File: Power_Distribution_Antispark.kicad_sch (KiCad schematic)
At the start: 155 parts, among them J1 5V Output 2, J10 +48V Battery Conn, J2 Adjustable Output, J3 Motor Conn, J4 12V Output 2, J5 Conn_01x14_Socket, J6 STM_Adj_En, J7 12V Output 1, J8 5V Output 1, J9 STM Conn, Q10 GSF3400, Q11 GSF3400, Q4 BUK9M42-60EX, Q6 GSF3400, Q7 G20P06K, Q8 BUK9M42-60EX, Q9 G20P06K, U1 MCP1792x-5002xDB, U10 INA181A3IDBVR, U11 INA181A3IDBVR, U12 INA181A3IDBVR, U13 INA181A3IDBVR, U15 SN74AHC1G02, U2 TPP60308-ES1R-S, U3 TPP60308-ES1R-S, U4 TPP60308-ES1R-S, U6 TLV74033PDBVR, U7 MCP6L01Rx-xOT, U8 INA181A3IDBVR, U9 INA181A3IDBVR

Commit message: schematic for review
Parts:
- removed F6: Fuse, symbol Device:Fuse
- added F5: 0679L9150-05, CustomFootprintLibrary:FUSC6125X279N-0679L9150-05, symbol CustomLibrary:0679L9150-05
- L1: value 8.2uH -> 6.8uH
- L2: value 8.2uH -> 15uH; footprint (none) -> CustomFootprintLibrary:IND_AMRM00101040_PUL-AMRM00101040150MA1
- L4: value 8.2uH -> 18uH
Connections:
- net +48V: now also F5.1
- net at D15.2 (A): now also F5.2
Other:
- note added: "I_ripplecurrent = 0.3*I_outmax = 0.3*3.5 = 1.05 13.7uH -> 15uH"
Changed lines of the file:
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@@
 		)
 	)
+	(text "I_ripplecurrent = 0.3*I_outmax = 0.3*3.5 = 1.05\n13.7uH -> 15uH"
+		(exclude_from_sim no)
+		(at 189.992 132.588 0)
+		(effects
+			(font
+				(size 1.27 1.27)
+			)
+		)
+	)
 	(text "Vout=0.8*(1+R1/R2)"
 		(exclude_from_sim no)
@@
 	(wire
 		(pts
-			(xy 39.37 43.18) (xy 45.72 43.18)
+			(xy 31.75 43.18) (xy 38.1 43.18)
 		)
 		(stroke
@@
 			)
 		)
-		(property "Value" "8.2uH"
+		(property "Value" "18uH"
 			(at 179.07 285.75 90)
 			(effects
@@
 			)
 		)
-		(property "Datasheet" "~"
+		(property "Datasheet" "https://www.digikey.ca/en/products/detail/vishay-dale/IFDC5050HZER180M/22475119"
 			(at 179.07 288.29 0)
 			(effects
@@
 			)
 		)
-		(property "Description" "Inductor, small symbol"
+		(property "Description" "FIXED IND 18UH 6.6A 39 MOHM SMD"
 			(at 179.07 288.29 0)
 			(effects
@@
 	(symbol
 		(lib_id "power:+48V")
-		(at 39.37 43.18 0)
+		(at 31.75 43.18 0)
 		(unit 1)
 		(exclude_from_sim no)
@@
 		(fields_autoplaced yes)
 		(property "Reference" "#PWR077"
-			(at 39.37 46.99 0)
+			(at 31.75 46.99 0)
 			(effects
 				(font
@@
 		)
 		(property "Value" "+48V"
-			(at 39.37 38.1 0)
+			(at 31.75 38.1 0)
 			(effects
 				(font
@@
 		)
 		(property "Footprint" ""
-			(at 39.37 43.18 0)
+			(at 31.75 43.18 0)
 			(effects
 				(font
@@
 		)
 		(property "Datasheet" ""
-			(at 39.37 43.18 0)
+			(at 31.75 43.18 0)
 			(effects
 				(font
@@
 		)
 		(property "Description" "Power symbol creates a global label with name \"+48V\""
-			(at 39.37 43.18 0)
+			(at 31.75 43.18 0)
 			(effects
 				(font
@@
 			)
 		)
-		(property "Value" "8.2uH"
+		(property "Value" "6.8uH"
 			(at 194.31 213.36 90)
 			(effects
@@
 					(size 1.27 1.27)
 				)
-				(hide yes)
 			)
 		)
-		(property "Datasheet" "~"
+		(property "Datasheet" "https://www.digikey.ca/en/products/detail/laird-signal-integrity-products/MGAH06036R8M-10/16731123"
 			(at 194.31 215.9 0)
 			(effects
@@
 			)
 		)
-		(property "Description" "Inductor, small symbol"
+		(property "Description" "FIXED IND 6.8UH 5A 50 MOHM SMD"
 			(at 194.31 215.9 0)
 			(effects
@@
 	)
 	(symbol
+		(lib_id "CustomLibrary:0679L9150-05")
+		(at 45.72 43.18 0)
+		(unit 1)
+		(exclude_from_sim no)
+		(in_bom yes)
+		(on_board yes)
+		(dnp no)
+		(fields_autoplaced yes)
+		(property "Reference" "F5"
+			(at 45.72 36.83 0)
+			(effects
+				(font
+					(size 1.27 1.27)
+				)
+			)
+		)
+		(property "Value" "0679L9150-05"
+			(at 45.72 39.37 0)
+			(effects
+				(font
+					(size 1.27 1.27)
+				)
+			)
+		)
+		(property "Footprint" "CustomFootprintLibrary:FUSC6125X279N-0679L9150-05"
+			(at 45.72 43.18 0)
+			(effects
+				(font
+					(size 1.27 1.27)
+				)
+				(justify bottom)
+				(hide yes)
+			)
+		)
+		(property "Datasheet" "https://www.digikey.ca/en/products/detail/bel-fuse-inc/0679L9150-05/5844044"
+			(at 45.72 43.18 0)
+			(effects
+				(font
+					(size 1.27 1.27)
+				)
+				(hide yes)
+			)
+		)
+		(property "Description" "FUSE BRD MNT 15A 125VAC/VDC 2SMD"
+			(at 45.72 43.18 0)
+			(effects
+				(font
+					(size 1.27 1.27)
+				)
+				(hide yes)
+			)
+		)
+		(property "PARTREV" "0679H Apr2019"
+			(at 45.72 43.18 0)
+			(effects
+				(font
+					(size 1.27 1.27)
+				)
+				(justify bottom)
+				(hide yes)
+			)
+		)
+		(property "MANUFACTURER" "BELFUSE"
+			(at 45.72 43.18 0)
+			(effects
+				(font
+					(size 1.27 1.27)
+				)
+				(justify bottom)
+				(hide yes)
+			)
+		)
+		(property "MAXIMUM_PACKAGE_HEIGHT" "2.79mm"
+			(at 45.72 43.18 0)
+			(effects
+				(font
+					(size 1.27 1.27)
+				)
+				(justify bottom)
+				(hide yes)
+			)
+		)
+		(property "STANDARD" "IPC-7351B"
+			(at 45.72 43.18 0)
+			(effects
+				(font
+					(size 1.27 1.27)
+				)
+				(justify bottom)
+				(hide yes)
+			)
+		)
+		(pin "1"
+		)
+		(pin "2"
+		)
+		(instances
+			(project ""
+				(path "/5e8a89a4-9381-43c9-9195-b0d86b17c24c"
+					(reference "F5")
+					(unit 1)
+				)
+			)
+		)
+	)
+	(symbol
 		(lib_id "Connector_Generic:Conn_01x06")
 		(at 210.82 379.73 0)
@@
 	)
 	(symbol
-		(lib_id "Device:Fuse")
-		(at 49.53 43.18 90)
-		(unit 1)
-		(exclude_from_sim no)
-		(in_bom yes)
-		(on_board yes)
-		(dnp no)
-		(fields_autoplaced yes)
-		(property "Reference" "F6"
-			(at 49.53 36.83 90)
-			(effects
-				(font
-					(size 1.27 1.27)
-				)
-			)
-		)
-		(property "Value" "Fuse"
-			(at 49.53 39.37 90)
-			(effects
-				(font
-					(size 1.27 1.27)
-				)
-			)
-		)
-		(property "Footprint" ""
-			(at 49.53 44.958 90)
-			(effects
-				(font
-					(size 1.27 1.27)
-				)
-				(hide yes)
-			)
-		)
-		(property "Datasheet" "https://www.digikey.ca/en/products/detail/bel-fuse-inc/0679L9150-05/5844044"
-			(at 49.53 43.18 0)
-			(effects
-				(font
-					(size 1.27 1.27)
-				)
-				(hide yes)
-			)
-		)
-		(property "Description" "FUSE BRD MNT 15A 125VAC/VDC 2SMD"
-			(at 49.53 43.18 0)
-			(effects
-				(font
-					(size 1.27 1.27)
-				)
-				(hide yes)
-			)
-		)
-		(pin "1"
-		)
-		(pin "2"
-		)
-		(instances
-			(project "Power_Distribution_Antispark"
-				(path "/5e8a89a4-9381-43c9-9195-b0d86b17c24c"
-					(reference "F6")
-					(unit 1)
-				)
-			)
-		)
-	)
-	(symbol
 		(lib_id "Device:R_Small_US")
 		(at 198.12 332.74 0)
@@
 			)
 		)
-		(property "Value" "8.2uH"
+		(property "Value" "15uH"
 			(at 187.96 139.7 90)
 			(effects
@@
 			)
 		)
-		(property "Footprint" ""
+		(property "Footprint" "CustomFootprintLibrary:IND_AMRM00101040_PUL-AMRM00101040150MA1"
 			(at 187.96 142.24 0)
 			(effects
@@
 			)
 		)
-		(property "Datasheet" "~"
+		(property "Datasheet" "https://www.digikey.ca/en/products/detail/pulse-electronics/AMRM00101040150MA1/21407862"
 			(at 187.96 142.24 0)
 			(effects
@@
 			)
 		)
-		(property "Description" "Inductor, small symbol"
+		(property "Description" "FIXED IND 15UH 6A 45 MOHM SMD"
 			(at 187.96 142.24 0)
 			(effects

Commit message: schematic fixed precharge logic
still need to spec inverter
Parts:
- removed R1: 1K, Resistor_SMD:R_0201_0603Metric, symbol Device:R_Small_US
- removed R3: 100K, Resistor_SMD:R_0201_0603Metric, symbol Device:R_Small_US
- removed R4: 20K, Resistor_SMD:R_0201_0603Metric, symbol Device:R_Small_US
- removed R63: 30K, Resistor_SMD:R_0201_0603Metric, symbol Device:R_Small_US
- added C46: 100nF, Capacitor_SMD:C_0201_0603Metric, symbol Device:C_Small
- added R38: 13K, Resistor_SMD:R_0201_0603Metric, symbol Device:R_Small_US
- added R39: 20K, Resistor_SMD:R_0201_0603Metric, symbol Device:R_Small_US
- added U5: 74AHC1G04, symbol 74xGxx:74AHC1G04
- R5: value 30K -> 13K
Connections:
- net +5V_PC: now also C46.1, U5.5 (VCC)
- net GND: now also C46.2, U5.3 (GND); no longer R6.1
- net at Q7.1 (G), R6.2: now also R5.2; no longer Q4.5 (D), R5.1
- net at D15.1 (K), D16.1 (K), Q7.3 (S)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: now also R5.1, R38.1; no longer R5.2
- net at Q8.5 (D): now also R39.1; no longer Q9.1 (G)
- net at Q4.4 (G): now also U5.4
- net Vamp renamed PC_Done
- net PC_Done: now also U5.2
- new net: Q4.5 (D), R6.1
- new net: Q9.1 (G), R38.2, R39.2
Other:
- note added: "Main Switch PC_Done = 0 (not done) Q8 recieves a 0 -> Q8 is open Q9 recieves a 1 -> Q9 is open - PC_Done = 1 (done) Q8 recieves a 1 -> Q8 is closed Q9 recieves a 0 -> Q9 is closed"
- note added: "Precharge Switch PC_Done = 0 (not done) -> invert -> 1 Q4 recieves a 1 -> Q4 is closed Q7 recieves a 0 -> Q7 is closed - PC_Done = 1 (done) -> invert -> 0 Q4 recieves a 0 -> Q4 is open Q7 recieves a 1 -> Q7 is open"
- note added: "voltage divider at Q7/Q9 gate to set Vsg (PMOS)<20"
- note removed: "voltage divider at Q7/Q9 gate to limit Vgs"
- moved on the sheet: C1, C17, C18, C2, C21, C22, D13, D14, D15, D16, D17, F4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

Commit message: updated connectors and inverter
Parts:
- removed J10: +48V Battery Conn, symbol Connector_Generic:Conn_01x06
- removed J3: Motor Conn, CustomFootprintLibrary:CONN_DME-02-S-P-S_ADM, symbol Connector:Conn_01x02_Socket
- removed U5: 74AHC1G04, symbol 74xGxx:74AHC1G04
- removed U6: TLV74033PDBVR, CustomFootprintLibrary:TLV74033PDBVR, symbol CustomSymbols:TLV74033PDBVR
- added J10: Motor Conn, CustomFootprintLibrary:AMASS_XT60PW-F, symbol CustomLibrary:XT60PW-F
- added J11: +48V Battery Conn, CustomFootprintLibrary:AMASS_XT60PW-F, symbol CustomLibrary:XT60PW-F
- added U14: TLV74033PDBVR, CustomFootprintLibrary:TLV74033PDBVR, symbol CustomLibrary:TLV74033PDBVR
- added U6: 74LVC1G14GW_125, CustomFootprintLibrary:SOT353_NEX, symbol CustomLibrary:74LVC1G14GW_125
- U2, U3, U4: footprint CustomFootprint:TPP60308-ES1R-S -> CustomFootprintLibrary:TPP60308-ES1R-S
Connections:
- net +3V3: now also U14.5 (OUT)
- net +48V: now also J10.1 (P), J11.1 (P)
- net +5V: now also U14.1 (IN)
- net +5V_PC: now also U14.3 (EN), U6.5 (VCC)
- net GND: now also J10.2 (N), J10.SH1 (SHIELD), J10.SH2 (SHIELD), J11.2 (N), J11.SH1 (SHIELD), J11.SH2 (SHIELD), U14.2 (GND), U6.3 (GND)
- net PC_Done: now also U6.2 (In)
- net at Q4.4 (G): now also U6.4 (Out)

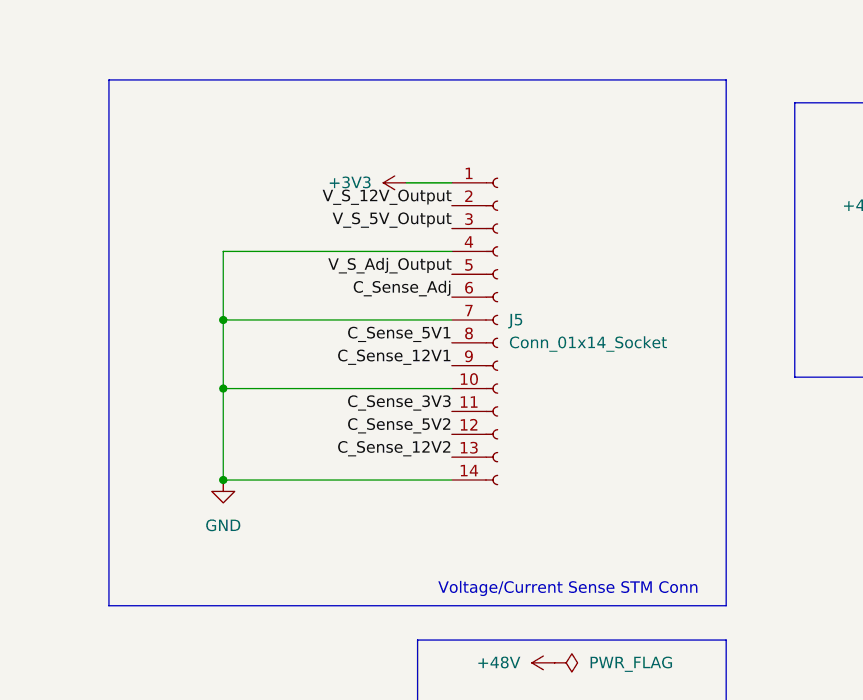
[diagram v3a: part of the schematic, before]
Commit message: updated connectors
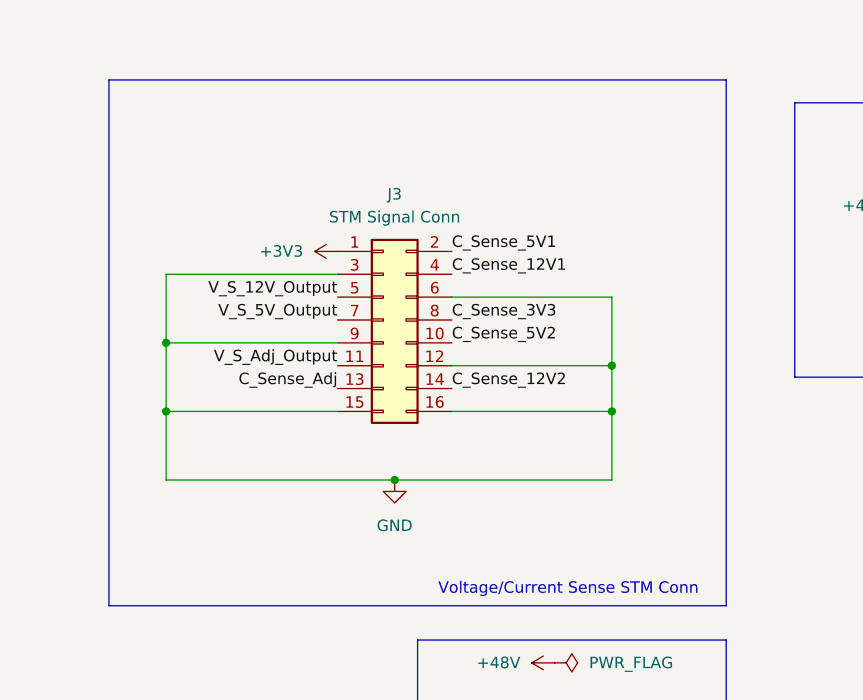
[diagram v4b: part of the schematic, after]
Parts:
- removed J5: Conn_01x14_Socket, Connector_PinSocket_2.54mm:PinSocket_1x14_P2.54mm_Vertical, symbol Connector:Conn_01x14_Socket
- added J3: STM Signal Conn, CustomFootprintLibrary:ADAM_PH2-08-UA, symbol Connector_Generic:Conn_02x08_Odd_Even
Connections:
- net +3V3: now also J3.1 (Pin_1)
- net C_Sense_12V1: now also J3.4 (Pin_4)
- net C_Sense_12V2: now also J3.14 (Pin_14)
- net C_Sense_3V3: now also J3.8 (Pin_8)
- net C_Sense_5V1: now also J3.2 (Pin_2)
- net C_Sense_5V2: now also J3.10 (Pin_10)
- net C_Sense_Adj: now also J3.13 (Pin_13)
- net GND: now also J3.12 (Pin_12), J3.15 (Pin_15), J3.16 (Pin_16), J3.3 (Pin_3), J3.6 (Pin_6), J3.9 (Pin_9)
- net V_S_12V_Output: now also J3.5 (Pin_5)
- net V_S_5V_Output: now also J3.7 (Pin_7)
- net V_S_Adj_Output: now also J3.11 (Pin_11)

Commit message: schematic update
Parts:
- removed C18, C30, C35, C37, C39, C40, C41: 1uF, Capacitor_SMD:C_0201_0603Metric, symbol Device:C_Small
- removed C21, C24, C25, C26, C28, C29, C31, C32, C34, C46: 100nF, Capacitor_SMD:C_0201_0603Metric, symbol Device:C_Small
- removed C36, C38: 2.2uF, Capacitor_SMD:C_0805_2012Metric, symbol Device:C_Small
- removed C42: 39pF, Capacitor_SMD:C_0201_0603Metric, symbol Device:C_Small
- removed C43: 6.8nF, Capacitor_SMD:C_0201_0603Metric, symbol Device:C_Small
- removed C44, C45: 47uF, Capacitor_SMD:C_0201_0603Metric, symbol Device:C_Small
- removed D12, D16: SMCJ48CA/TR13, Diode_SMD:D_SMC, symbol Diode:DSB5712
- removed D15, D8: MBRD20100, Package_TO_SOT_SMD:TO-252-3_TabPin2, symbol Diode:1N4148WT
- removed D17: PNU650150AEJJ, Package_TO_SOT_SMD:TO-263-3_TabPin2, symbol Diode:1N4148WT
- removed D6: SS56, Diode_SMD:D_SMA, symbol Diode:SB160
- removed F1: Fuse, Fuse:Fuse_0603_1608Metric, symbol Device:Fuse
- removed F5: 0679L9150-05, CustomFootprintLibrary:FUSC6125X279N-0679L9150-05, symbol CustomLibrary:0679L9150-05
- removed J1: 5V Output 2, CustomFootprintLibrary:M20-9990246, symbol CustomLibrary:M20-9990246
- removed J2: Adjustable Output, CustomFootprintLibrary:M20-9990246, symbol CustomLibrary:M20-9990246
- removed J4: 12V Output 2, CustomFootprintLibrary:M20-9990246, symbol CustomLibrary:M20-9990246
- removed J6: STM_Adj_En, symbol Connector_Generic:Conn_01x06
- removed J7: 12V Output 1, CustomFootprintLibrary:M20-9990246, symbol CustomLibrary:M20-9990246
- removed J8: 5V Output 1, CustomFootprintLibrary:M20-9990246, symbol CustomLibrary:M20-9990246
- removed J9: STM Conn, CustomFootprintLibrary:M20-9990246, symbol CustomLibrary:M20-9990246
- removed L4: 18uH, symbol Device:L_Small
- removed Q10, Q11, Q6: GSF3400, Package_TO_SOT_SMD:SOT-23-3, symbol Simulation_SPICE:NMOS
- removed Q4, Q8: BUK9M42-60EX, Package_TO_SOT_SMD:LFPAK33, symbol Transistor_FET:BUK9M42-60EX
- removed Q7, Q9: G20P06K, Package_TO_SOT_SMD:TO-252-3_TabPin2, symbol Transistor_FET:SUD08P06-155L
- removed R12, R29, R30: 10.5K, Resistor_SMD:R_0201_0603Metric, symbol Device:R_Small_US
- removed R15, R21, R7, R8: 1K, Resistor_SMD:R_0201_0603Metric, symbol Device:R_Small_US
- removed R31, R44, R45, R46, R47, R48: 0.006, Resistor_SMD:R_0805_2012Metric, symbol Device:R_Small_US
- removed R32: DTO025C100R0JTE3, CustomFootprintLibrary:RES_DTO025_VIS, symbol CustomLibrary:DTO025C100R0JTE3
- removed R35: 49.9, Resistor_SMD:R_0201_0603Metric, symbol Device:R_Small_US
- removed R36: 160K, Resistor_SMD:R_0201_0603Metric, symbol Device:R_Small_US
- removed R37, R38, R5: 13K, Resistor_SMD:R_0201_0603Metric, symbol Device:R_Small_US
- removed R39, R6: 20K, Resistor_SMD:R_0201_0603Metric, symbol Device:R_Small_US
- removed R51, R69, R70: 10K, Resistor_SMD:R_0201_0603Metric, symbol Device:R_Small_US
- removed R54: 0, Resistor_SMD:R_0201_0603Metric, symbol Device:R_Small_US
- removed R55: 5900, Resistor_SMD:R_0201_0603Metric, symbol Device:R_Small_US
- removed R57: 30.9K, Resistor_SMD:R_0201_0603Metric, symbol Device:R_Small_US
- removed R62: 100K, Resistor_SMD:R_0201_0603Metric, symbol Device:R_Small_US
- removed R65: 3300, Resistor_SMD:R_0201_0603Metric, symbol Device:R_Small_US
- removed R66: 220, Resistor_SMD:R_0201_0603Metric, symbol Device:R_Small_US
- removed R67: 2000, Resistor_SMD:R_0201_0603Metric, symbol Device:R_Small_US
- removed R68: 62, Resistor_SMD:R_0201_0603Metric, symbol Device:R_Small_US
- removed U10, U11, U12, U13, U9: INA181A3IDBVR, CustomFootprintLibrary:INA181A3IDBVR, symbol CustomLibrary:INA181A3IDBVR
- removed U15: SN74AHC1G02, Package_TO_SOT_SMD:SOT-353_SC-70-5, symbol 74xGxx:74AHC1G02
- removed U4: TPP60308-ES1R-S, CustomFootprintLibrary:TPP60308-ES1R-S, symbol CustomLibrary:TPP60308-ES1R-S
- removed U6: 74LVC1G14GW_125, CustomFootprintLibrary:SOT353_NEX, symbol CustomLibrary:74LVC1G14GW_125
- removed U7: MCP6L01Rx-xOT, Package_TO_SOT_SMD:SOT-23-5, symbol Amplifier_Operational:MCP6L01Rx-xOT
- added C20: 1uF, Capacitor_SMD:C_0201_0603Metric, symbol Device:C_Small
- added D12, D13: MM3Z16-AQ, Diode_SMD:D_SOD-323F, symbol Diode:BZT52Bxx
- added D5: MBRD20100, Package_TO_SOT_SMD:TO-252-3_TabPin2, symbol Diode:1N4148WT
- added D6: SMCJ48CA/TR13, Diode_SMD:D_SMC, symbol Diode:DSB5712
- added D9: PNU650150AEJJ, Package_TO_SOT_SMD:TO-263-3_TabPin2, symbol Diode:1N4148WT
- added F1: 0679L9150-05, CustomFootprintLibrary:FUSC6125X279N-0679L9150-05, symbol CustomLibrary:0679L9150-05
- added Q1, Q3: BUK9M42-60EX, Package_TO_SOT_SMD:LFPAK33, symbol Transistor_FET:BUK9M42-60EX
- added Q2, Q4: G20P06K, Package_TO_SOT_SMD:TO-252-3_TabPin2, symbol Transistor_FET:SUD08P06-155L
- added R1: 1K, Resistor_SMD:R_0201_0603Metric, symbol Device:R_Small_US
- added R15: DTO025C100R0JTE3, CustomFootprintLibrary:RES_DTO025_VIS, symbol CustomLibrary:DTO025C100R0JTE3
- added R16, R24: 10K, Resistor_SMD:R_0201_0603Metric, symbol Device:R_Small_US
- added R3: 20K, Resistor_SMD:R_0201_0603Metric, symbol Device:R_Small_US
- added R32: 0.006, Resistor_SMD:R_0805_2012Metric, symbol Device:R_Small_US
- added R4: 13K, Resistor_SMD:R_0201_0603Metric, symbol Device:R_Small_US
- added U1: 74LVC1G14GW_125, CustomFootprintLibrary:SOT353_NEX, symbol CustomLibrary:74LVC1G14GW_125
- added U4: LM331AU-S5TR, CustomFootprintLibrary:S5TSOT23-5-A_TPK, symbol CustomLibrary:LM331AU-S5TR
- C17: value 1uF -> 100nF
- C22, C27: value 100nF -> 1uF
- R10: value 1.5K -> 20K
- R11, R33: value 1K -> 1.1K
- R2: value 1K -> 100K
- R23: value 1.5K -> 1.1K
- R34: value 1K -> 1.3K
- R9: value 1K -> 13K
- renumbered C10 to C1, C5 to C10, C14 to C11, C6 to C12, C15 to C13, C8 to C14, C16 to C15, C9 to C16, C33 to C18, C23 to C19, C3 to C2, C1 to C21, C2 to C23, C11 to C3, C19 to C5, C20 to C6, C12 to C7, C7 to C8, C13 to C9, D5 to D1, D13 to D10, D14 to D11, D7 to D2, D10 to D3, D11 to D4, D2 to D7, D1 to D8, J3 to J1, J11 to J5, J10 to J6, L2 to L1, L1 to L2, R49 to R12, R50 to R14, R27 to R17, R28 to R18, R14 to R19, R16 to R20, R17 to R21, R18 to R22, R41 to R25, R42 to R26, R22 to R27, R24 to R28, R25 to R5, R19 to R6, R26 to R7, R20 to R8, U3 to U2, U2 to U3, U14 to U5, U1 to U6
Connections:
- net +3V3: now also C22.1
- net +48V: now also F1.1
- net +5V: now also C20.1; no longer C17.1
- net +5V_PC: now also C17.1, C27.1, U1.5 (VCC), U4.5 (V+); no longer C22.1
- net GND: now also R11.1, R2.1, R34.2, C20.2, D6.2 (A), Q1.1 (S), Q1.2 (S), Q1.3 (S), Q3.1 (S), Q3.2 (S), Q3.3 (S), U1.3 (GND), U4.2 (V-); no longer J1.15 (Pin_15), J1.16 (Pin_16), R10.1, R13.2, R34.1, R9.1, U8.4 (IN-)
- net MotorConn: now also D9.1 (K), Q2.2 (D)
- net PC_Done: now also R1.1, R24.2, U1.2 (In), U4.4 (OUT); no longer R13.1, R2.1
- net V_S_12V_Output: now also R25.2, R26.1
- net V_S_5V_Output: now also R27.1, R28.2
- net PreChargeSense: now reaches U8.3 (IN+)
- net PreChargeSense: now also R33.1, R34.1, R32.1
- net at R23.2: now also R16.1, U4.3 (IN+)
- net at R11.2: now also R13.1, R24.1, U4.1 (IN-)
- net at R9.2: now also R10.2, D13.2 (A), Q4.1 (G)
- net at R33.2: now also R15.2, R16.2; no longer R34.2
- net at R2.2: now also Q1.4 (G), R1.2
- net C_Sense_Adj renamed C_Sense_3V3_STM
- net C_Sense_3V3_STM: no longer U8.1 (OUT)
- net V_S_Adj_Output renamed C_Sense_5V3
- net C_Sense_5V3: no longer R33.1
- new net: Q1.5 (D), R3.1
- new net: D12.2 (A), Q2.1 (G), R3.2, R4.2
- new net: D5.2 (A), F1.2
- new net: Q3.5 (D), R10.1
- new net: D12.1 (K), D13.1 (K), D5.1 (K), D6.1 (K), Q2.3 (S), Q4.3 (S), R4.1, R9.1
- new net: Q4.2 (D), R13.2, R15.1
- new net: Q3.4 (G), U1.4 (Out)
- new net C_Sense_12V3: J1.16 (Pin_16)
- new net PreChargeSenseEnd: D9.2 (A), R32.2, U8.4 (IN-)
- new net PreCharge_Sense: J1.15 (Pin_15), U8.1 (OUT)
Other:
- added sheet CSense12V_1 (CSense.kicad_sch)
- added sheet CSense12V_2 (CSense.kicad_sch)
- added sheet CSense12V_3 (CSense.kicad_sch)
- added sheet CSense3V3STM (CSense.kicad_sch)
- added sheet CSense3V3_2 (CSense.kicad_sch)
- added sheet CSense5V_1 (CSense.kicad_sch)
- added sheet CSense5V_2 (CSense.kicad_sch)
- added sheet CSense5V_3 (CSense.kicad_sch)
- note added: "(48-5)(10nA+4uA+300uA+(2*200uA)+(6*260uA))= ~0.0946W"
- note added: "Comparator outputs 1 when precharge is done"
- note added: "Max Vin = 48V Vsupply = 5V V+/- in max = 5v +- 0.3v = 5.5/-0.3V Voltage divide inputs by 10x 48V/10 = ~4.8"
- note added: "PreCharge Current Sense"
- note removed: "100 = 5V 110 = 12V 111 = 24V Default configuration is for 12V"
- note removed: "48V -> 24V/12V/5V"
- note removed: "Max Vdiff = 48V NOR gate max input = 7V --> reduce by factor of 8 Voltage divide opamp inputs by 8x Then opamp gain of 1 into logic gates"
- note removed: "STM Enable Conn for Adjustable Buck"
- note removed: "V_adj steps down by a factor of 8"
- note removed: "Vout=0.8*(1+R1/R2)"
- moved on the sheet: C21, C23, D10, D11, F4, J1, J5, J6, U5, U6

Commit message: changed ldo to buck
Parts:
- removed D10: MBRD20100, Package_TO_SOT_SMD:TO-252-3_TabPin2, symbol Diode:1N4148WT
- removed D11: SMCJ48CA/TR13, Diode_SMD:D_SMC, symbol Diode:DSB5712
- removed F4: Fuse, Fuse:Fuse_0603_1608Metric, symbol Device:Fuse
- removed U6: MCP1792x-5002xDB, Package_TO_SOT_SMD:SOT-223-3_TabPin2, symbol Regulator_Linear:MCP1792x-5002xDB
- added C24: 100nF, Capacitor_SMD:C_0201_0603Metric, symbol Device:C_Small
- added C25: 15uF, Capacitor_SMD:C_0201_0603Metric, symbol Device:C_Small
- added L3: 82uH, CustomFootprintLibrary:IND_ASPI-4030S-820M-T, symbol Device:L_Small
- added R29: 118K, Resistor_SMD:R_0201_0603Metric, symbol Device:R_Small_US
- added R30: 22.1K, Resistor_SMD:R_0201_0603Metric, symbol Device:R_Small_US
- added U6: LMR51603XDBVR, CustomFootprintLibrary:DBV0006A-MFG, symbol CustomLibrary:LMR51603XDBVR
- C23: value 2.2uF -> 100nF; footprint Capacitor_SMD:C_0805_2012Metric -> Capacitor_SMD:C_0201_0603Metric
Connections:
- net +48V: now also C21.1, U6.4 (EN), U6.5 (VIN)
- net +5V_PC: now also C24.1, C25.1, L3.2, R29.2; no longer C23.1
- net GND: now also C24.2, C25.2, R30.1, U6.2 (GND); no longer C23.2
- new net: R29.1, R30.2, U6.3 (FB)
- new net: C23.1, U6.1 (CB)
- new net: C23.2, L3.1, U6.6 (SW)
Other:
- note added: "48V->5V Precharge Enable Control"
- note removed: "(48-5)(10nA+4uA+300uA+(2*200uA)+(6*260uA))= ~0.0946W"
- note removed: "48V->5V Precharge LDO"
- moved on the sheet: C20, C22, J1, J5, J6, U5
